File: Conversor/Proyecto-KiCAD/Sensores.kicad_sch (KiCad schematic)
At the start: 27 parts, among them U1 OPA365xxD, U16 74LS06, U2 ISO7242C, U3 LM5056APMH/NOPB, U4 TMCS1100A4

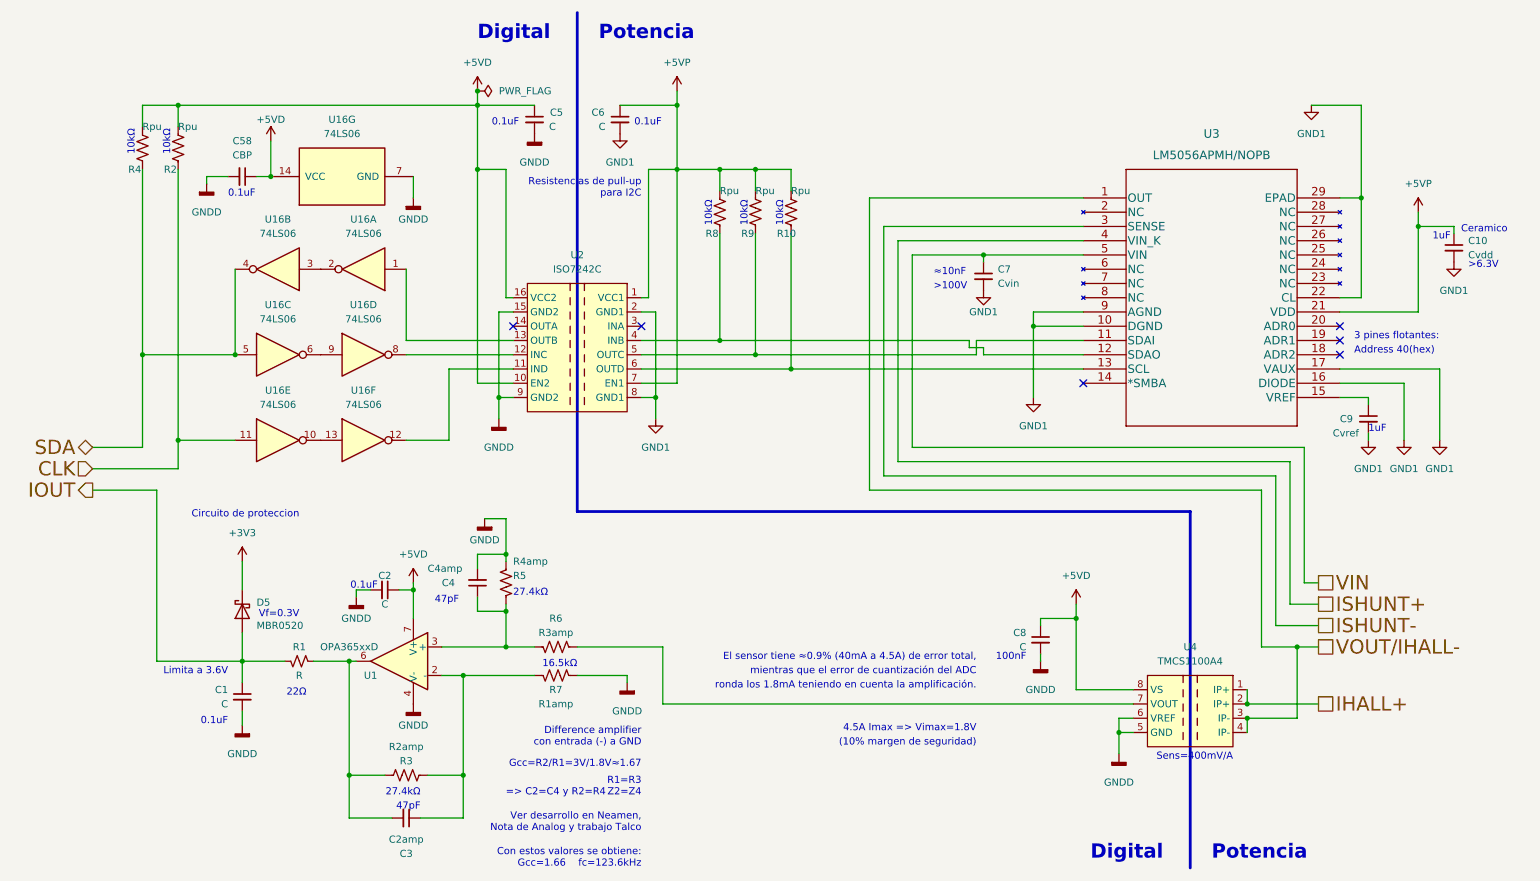
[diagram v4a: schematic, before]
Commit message: Agregar resistencias de pull-up faltantes
- Agregar resistencias de pull-up a la salida de cada inversor del
74LS06
- Crear plano de U5V en la capa superior alrededor del FTDI
- Ponerle los valores a los componentes para poder generar correctamente
el BOM (Bill of Materials)
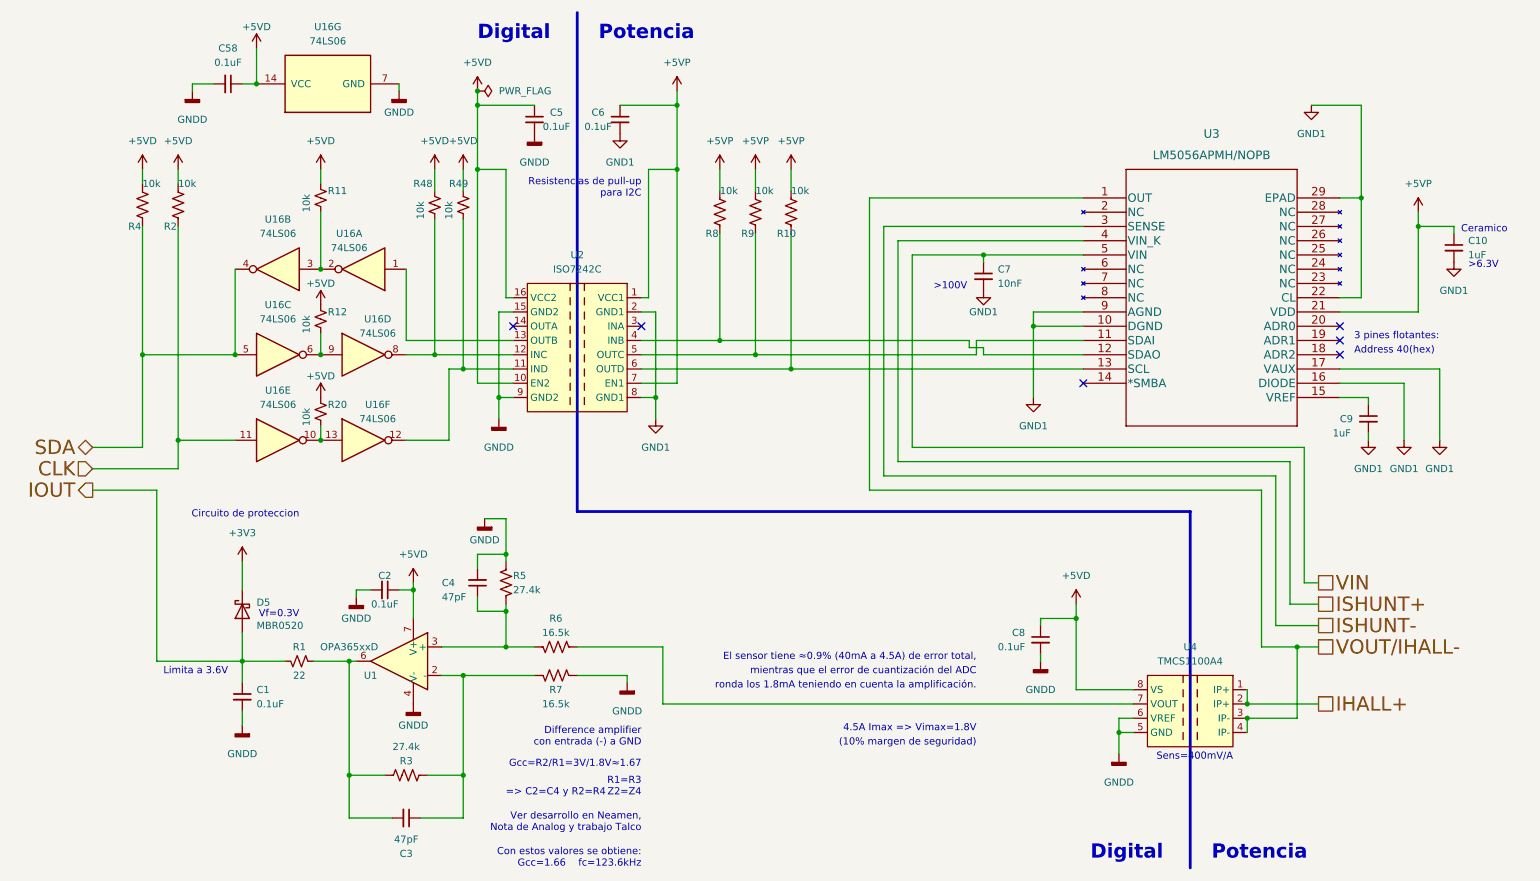
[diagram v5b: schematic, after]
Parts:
- added R11, R12, R20, R48, R49: 10k, Resistor_SMD:R_0805_2012Metric_Pad1.20x1.40mm_HandSolder, symbol Device:R_Small_US
- C1, C2, C5, C6, C8: value C -> 0.1uF
- C10: value Cvdd -> 1uF
- C3: value C2amp -> 47pF
- C4: value C4amp -> 47pF
- C58: value CBP -> 0.1uF
- C7: value Cvin -> 10nF
- C9: value Cvref -> 1uF
- R1: value R -> 22
- R10, R2, R4, R8, R9: value Rpu -> 10k
- R3: value R2amp -> 27.4k
- R5: value R4amp -> 27.4k
- R6: value R3amp -> 16.5k
- R7: value R1amp -> 16.5k
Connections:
- net +5VD: now also R11.1, R12.1, R20.1, R48.1, R49.1
- net at U16.8, U2.12 (INC): now also R48.2
- net at U16.6, U16.9: now also R12.2
- net at U16.12, U2.11 (IND): now also R49.2
- net at U16.10, U16.13: now also R20.2
- net at U16.2, U16.3: now also R11.2
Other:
- note removed: "0.1uF"
- note removed: "100nF"
- note removed: "10kΩ"
- note removed: "16.5kΩ"
- note removed: "1uF"
- note removed: "22Ω"
- note removed: "27.4kΩ"
- note removed: "47pF"
- note removed: "≈10nF"
- moved on the sheet: C58, R2, R4, U16G

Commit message: Eliminar resistencias de pull-up de SCL y SDAI
- Se pueden remover las Rpu del lado del sensor ya que las Rpu de esas
lineas estan del otro lado (la barrera de aislación proteje de daños).
La de SDAO tiene que quedar por la salida open-drain del LM5056.
- También cambiar las Rpu de 10k a 4k7, porque la capacidad del bus es
muy baja (un solo esclavo y pistas cortas). Así se disminuye es rise
time (Rpu*Cbus) a la mitad.
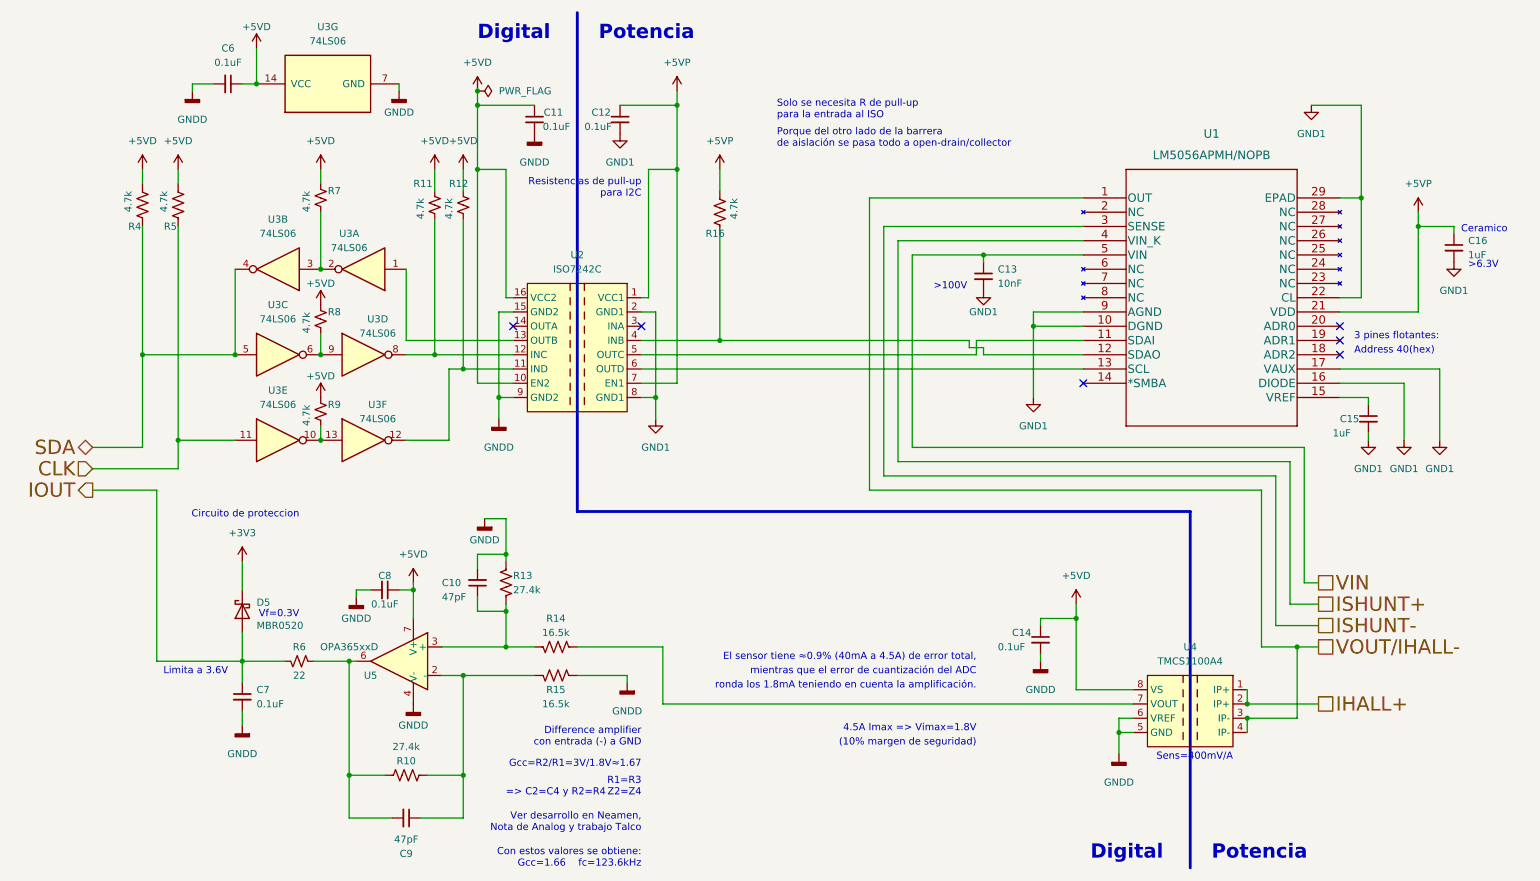
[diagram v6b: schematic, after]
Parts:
- removed R10, R9: 10k, Resistor_SMD:R_1206_3216Metric_Pad1.30x1.75mm_HandSolder, symbol Device:R_US
- R11: renamed from R48; value 10k -> 4.7k
- R12: renamed from R49; value 10k -> 4.7k
- R16: renamed from R8; value 10k -> 4.7k
- R4: value 10k -> 4.7k
- R5: renamed from R2; value 10k -> 4.7k
- R7: renamed from R11; value 10k -> 4.7k
- R8: renamed from R12; value 10k -> 4.7k
- R9: renamed from R20; value 10k -> 4.7k
- renumbered C4 to C10, C5 to C11, C6 to C12, C7 to C13, C8 to C14, C9 to C15, C10 to C16, C58 to C6, C1 to C7, C2 to C8, C3 to C9, R3 to R10, R5 to R13, R6 to R14, R7 to R15, R1 to R6, U3 to U1, U16 to U3, U1 to U5
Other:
- note added: "Porque del otro lado de la barrera de aislación se pasa todo a open-drain/collector"
- note added: "Solo se necesita R de pull-up para la entrada al ISO"

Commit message: Terminar el resto de los cambios de Jorge
- Capacitores electroliticos para el circuito de bootstrap, en paralelo
a los cerámicos
- Cambiar el I2C a 3V3 del lado digital
- Hacer la separacion de linea de datos de I2C del lado digital como en
la nota de aplicación SLYT403A
- Dejar el Vaux del LM5056A con un jumper por si acaso
- Lo mismo con la resistencia de dead-time RDT de los drivers, dejar una
footprint de resistencia SMD para poder cambiarlas de ser necesario
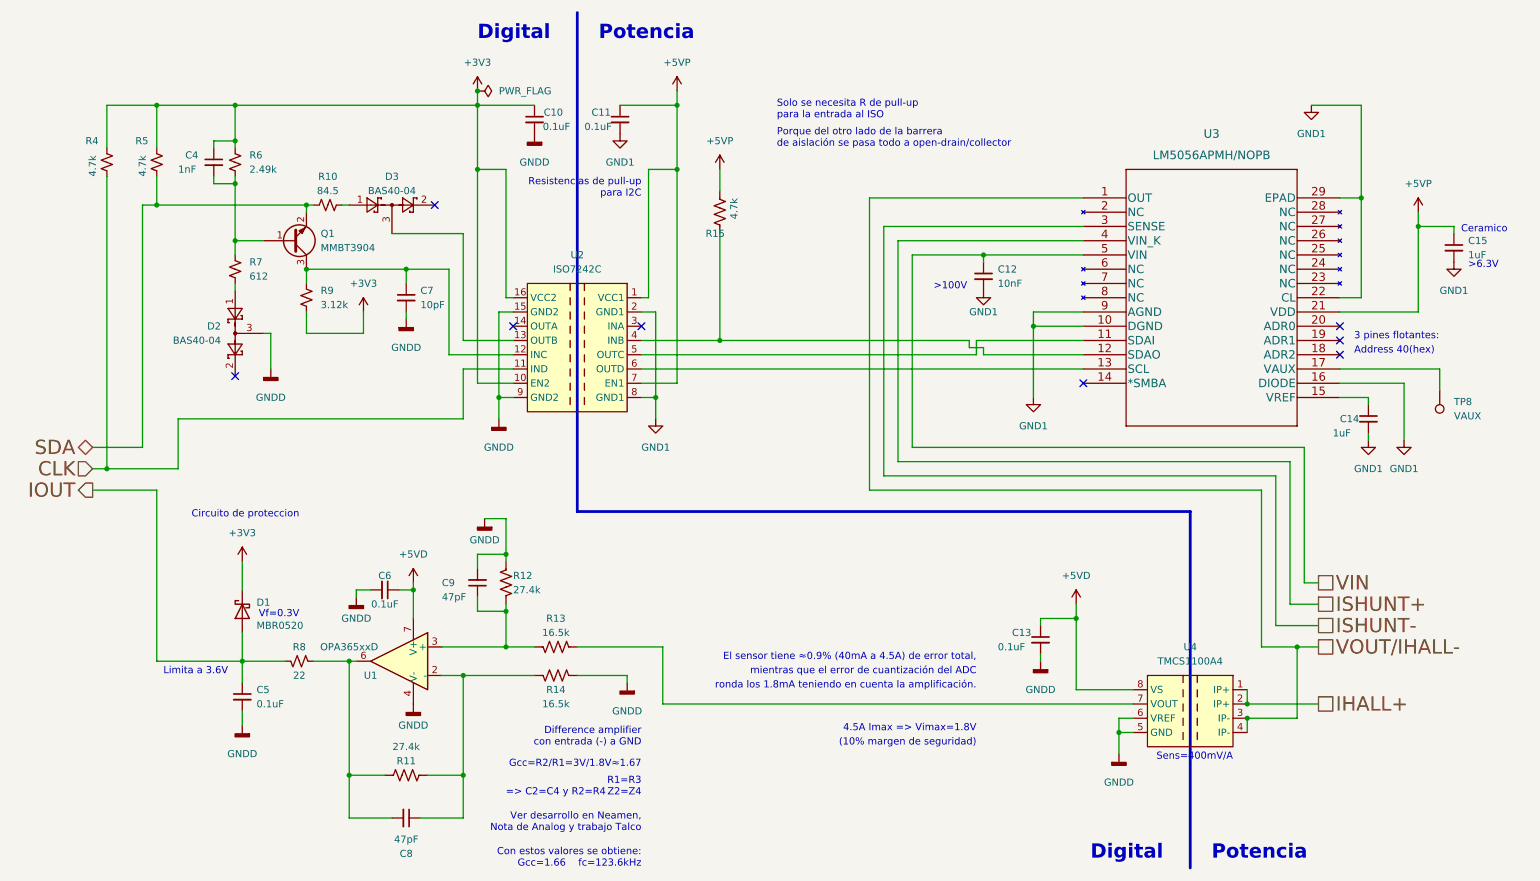
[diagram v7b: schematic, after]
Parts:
- removed C6: 0.1uF, Capacitor_SMD:C_1206_3216Metric_Pad1.33x1.80mm_HandSolder, symbol Device:C_Small
- removed R4, R5: 4.7k, Resistor_SMD:R_1206_3216Metric_Pad1.30x1.75mm_HandSolder, symbol Device:R_US
- removed R8: 4.7k, Resistor_SMD:R_0805_2012Metric_Pad1.20x1.40mm_HandSolder, symbol Device:R_Small_US
- removed U3: 74LS06, symbol 74xx:74LS06
- added C4: 1nF, Capacitor_SMD:C_1206_3216Metric_Pad1.33x1.80mm_HandSolder, symbol Device:C_Small
- added C7: 10pF, Capacitor_SMD:C_1206_3216Metric_Pad1.33x1.80mm_HandSolder, symbol Device:C_Small
- added D2, D3: BAS40-04, Package_TO_SOT_SMD:SOT-23, symbol Diode:BAS40-04
- added Q1: MMBT3904, Package_TO_SOT_SMD:SOT-23, symbol Transistor_BJT:MMBT3904
- added R10: 84.5, Resistor_SMD:R_1206_3216Metric_Pad1.30x1.75mm_HandSolder, symbol Device:R_Small_US
- added R6: 2.49k, Resistor_SMD:R_1206_3216Metric_Pad1.30x1.75mm_HandSolder, symbol Device:R_Small_US
- added TP8: VAUX, TestPoint:TestPoint_THTPad_2.0x2.0mm_Drill1.0mm, symbol Connector:TestPoint
- R4: renamed from R12; footprint Resistor_SMD:R_0805_2012Metric_Pad1.20x1.40mm_HandSolder -> Resistor_SMD:R_1206_3216Metric_Pad1.30x1.75mm_HandSolder
- R5: renamed from R11; footprint Resistor_SMD:R_0805_2012Metric_Pad1.20x1.40mm_HandSolder -> Resistor_SMD:R_1206_3216Metric_Pad1.30x1.75mm_HandSolder
- R7: value 4.7k -> 612; footprint Resistor_SMD:R_0805_2012Metric_Pad1.20x1.40mm_HandSolder -> Resistor_SMD:R_1206_3216Metric_Pad1.30x1.75mm_HandSolder
- R9: value 4.7k -> 3.12k; footprint Resistor_SMD:R_0805_2012Metric_Pad1.20x1.40mm_HandSolder -> Resistor_SMD:R_1206_3216Metric_Pad1.30x1.75mm_HandSolder
- renumbered C11 to C10, C12 to C11, C13 to C12, C14 to C13, C15 to C14, C16 to C15, C7 to C5, C8 to C6, C9 to C8, C10 to C9, D5 to D1, R10 to R11, R13 to R12, R14 to R13, R15 to R14, R16 to R15, R6 to R8, U5 to U1, U1 to U3
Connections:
- net +3V3: now also C10.1, R4.1, R5.1, R9.2, U2.10 (EN2), U2.16 (VCC2), C4.1, R6.1
- net +5VD: no longer C10.1, R4.1, R5.1, R7.1, R9.1, U2.10 (EN2), U2.16 (VCC2)
- net CLK: now also R4.2, U2.11 (IND)
- net GND1: no longer U3.17 (VAUX)
- net GNDD: now also C7.2, D2.3
- net SDA: now also R5.2, Q1.2 (E), R10.1
- net at U2.12 (INC): now also R9.1, C7.1, Q1.3 (C); no longer R5.2
- net at U2.13 (OUTB): now also D3.3
- net at R7.2: now also D2.1
- new net: TP8.1, U3.17 (VAUX)
- new net: D3.1, R10.2
- new net: C4.2, Q1.1 (B), R6.2, R7.1
- no-connect marks 6 -> 8
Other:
- moved on the sheet: R4, R5

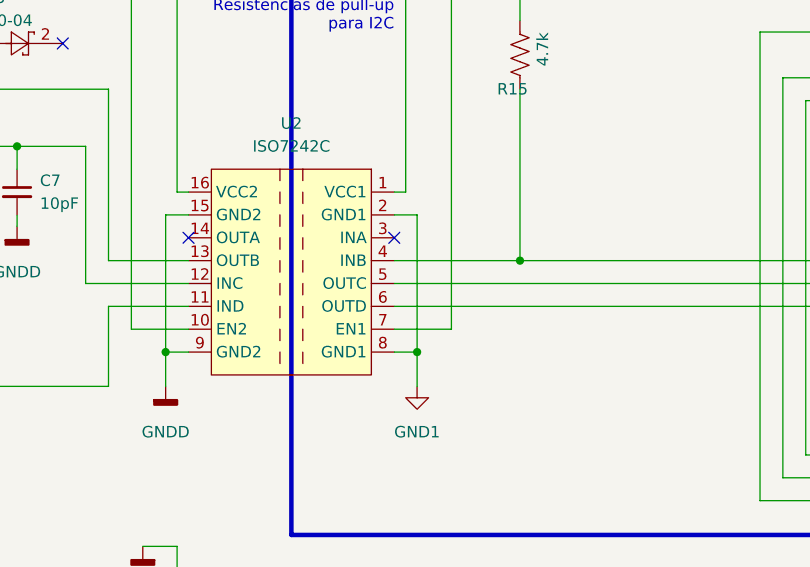
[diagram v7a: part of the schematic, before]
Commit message: Conectar la entrada en desuso del ISO a tierra
- Las entradas no se tienen que dejar flotantes. Salida flotante.
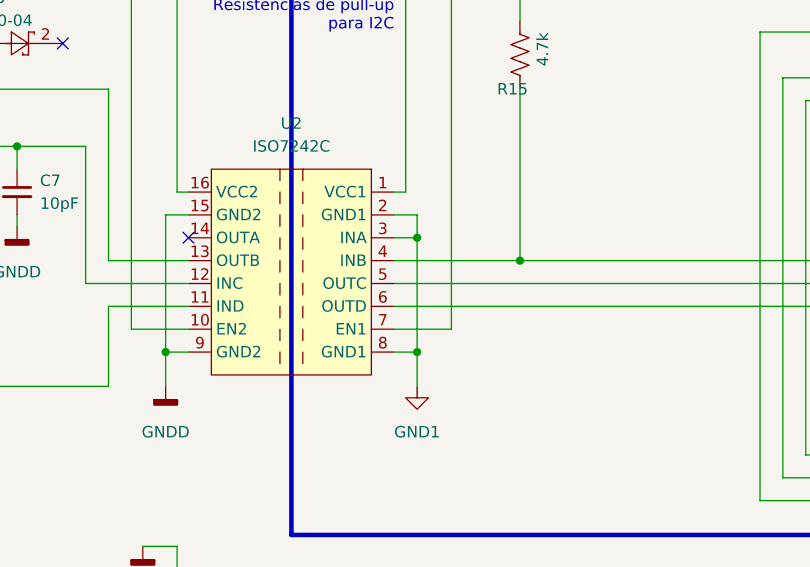
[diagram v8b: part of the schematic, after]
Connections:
- net GND1: now also U2.3 (INA)
- no-connect marks 8 -> 7
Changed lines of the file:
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@@
   (junction (at 256.54 45.72) (diameter 0) (color 0 0 0 0)
   )
+  (junction (at 130.81 68.58) (diameter 0) (color 0 0 0 0)
+  )
   (junction (at 99.06 40.64) (diameter 0) (color 0 0 0 0)
   )
@@
   )
   (no_connect (at 105.41 68.58))
-  (no_connect (at 128.27 68.58))
   (no_connect (at 91.44 46.99))
   (no_connect (at 55.88 77.47))
@@
     (stroke (width 0) (type default) (color 0 0 0 0))
   )
-  (wire (pts (xy 130.81 66.04) (xy 130.81 81.28))
+  (wire (pts (xy 130.81 66.04) (xy 130.81 68.58))
     (stroke (width 0) (type default) (color 0 0 0 0))
   )
   (wire (pts (xy 264.16 78.74) (xy 252.73 78.74))
+    (stroke (width 0) (type default) (color 0 0 0 0))
+  )
+  (wire (pts (xy 130.81 68.58) (xy 130.81 81.28))
     (stroke (width 0) (type default) (color 0 0 0 0))
   )
@@
     (stroke (width 0) (type default) (color 0 0 0 0))
   )
+  (wire (pts (xy 128.27 68.58) (xy 130.81 68.58))
+    (stroke (width 0) (type default) (color 0 0 0 0))
+  )
